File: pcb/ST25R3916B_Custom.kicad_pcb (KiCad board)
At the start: 2 copper layers, 40 x 40 mm, 12 parts

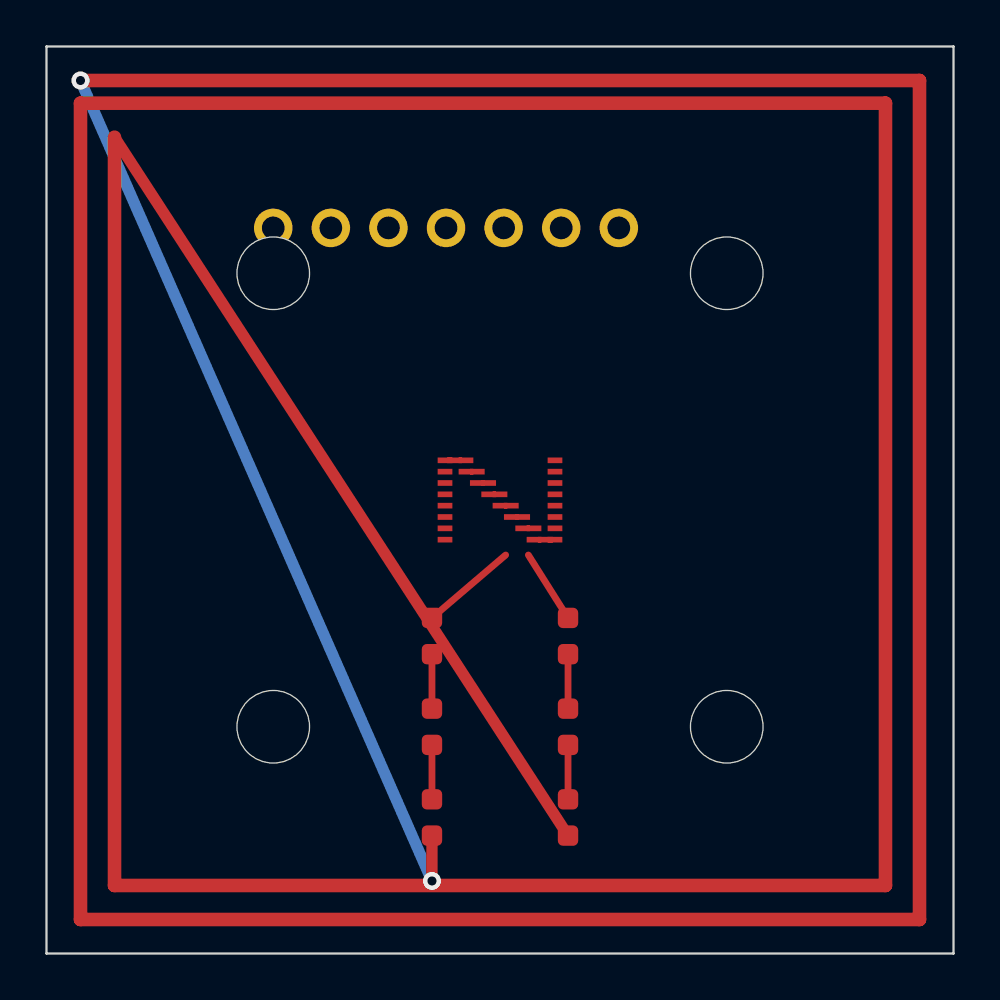
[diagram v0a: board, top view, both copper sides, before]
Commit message: feat(pcb): complete JLCPCB-ready PCB design with full PCBA outputs
- Fix generate_kicad.py: correct fp_text syntax for all footprints,
  add net declarations required by KiCad 7 parser
- Add all 22 SMD components with correct footprints and routing:
  RF matching network, crystal, LDO, bypass caps, SPI connector
- Replace broken legacy gerbers with clean kicad-cli exports
  (.gtl/.gbl/.gts/.gbs/.gto/.gbo/.gm1 + .drl)
- Add gerbers.zip ready for JLCPCB upload
- Add jlcpcb_bom.csv and jlcpcb_cpl.csv for PCBA ordering
- Update README with complete ordering instructions and pinout

Co-Authored-By: Claude Sonnet 4.6 <noreply@anthropic.com>
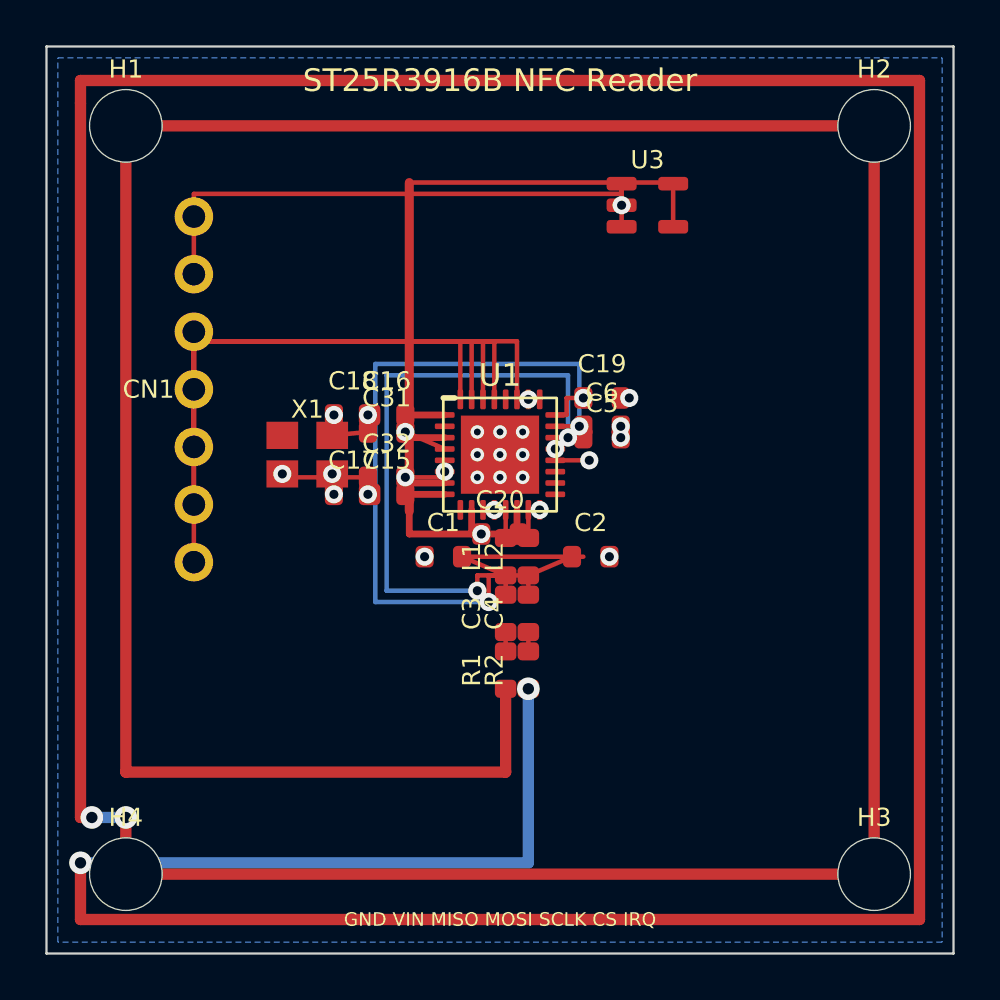
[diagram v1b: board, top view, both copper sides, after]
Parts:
- removed ? (x4): , MountingHole:MountingHole_3.2mm_M3
- removed ? (x6): , Resistor_SMD:R_0603_1608Metric
- removed ?: , Custom:ST25R3916B
- removed ?: , Connector_PinHeader_2.54mm:PinHeader_1x07_P2.54mm_Vertical
- added C1: 220pF, Resistor_SMD:R_0603_1608Metric, F.Cu at (117.5, 122.5)
- added C15: 100nF, Resistor_SMD:R_0603_1608Metric, F.Cu at (115.0, 119.8)
- added C16: 100nF, Resistor_SMD:R_0603_1608Metric, F.Cu at (115.0, 116.2)
- added C17: 2.2uF, Resistor_SMD:R_0603_1608Metric, F.Cu at (113.5, 119.8)
- added C18: 2.2uF, Resistor_SMD:R_0603_1608Metric, F.Cu at (113.5, 116.2)
- added C19: 10nF, Resistor_SMD:R_0603_1608Metric, F.Cu at (124.5, 115.5)
- added C2: 220pF, Resistor_SMD:R_0603_1608Metric, F.Cu at (124.0, 122.5)
- added C20: 10nF, Resistor_SMD:R_0603_1608Metric, F.Cu at (120.0, 121.5)
- added C3: 120pF, Resistor_SMD:R_0603_1608Metric, F.Cu at (120.2, 125.0)
- added C31: 12pF, Resistor_SMD:R_0603_1608Metric, F.Cu at (115.0, 117.0)
- added C32: 12pF, Resistor_SMD:R_0603_1608Metric, F.Cu at (115.0, 119.0)
- added C4: 120pF, Resistor_SMD:R_0603_1608Metric, F.Cu at (121.2, 125.0)
- added C5: 180pF, Resistor_SMD:R_0603_1608Metric, F.Cu at (124.5, 117.2)
- added C6: 180pF, Resistor_SMD:R_0603_1608Metric, F.Cu at (124.5, 116.8)
- added CN1: 7P-2.54mm, Connector_PinHeader_2.54mm:PinHeader_1x07_P2.54mm_Vertical, F.Cu at (106.5, 107.5)
- added H1: M3, MountingHole:MountingHole_3.2mm_M3, F.Cu at (103.5, 103.5)
- added H2: M3, MountingHole:MountingHole_3.2mm_M3, F.Cu at (136.5, 103.5)
- added H3: M3, MountingHole:MountingHole_3.2mm_M3, F.Cu at (136.5, 136.5)
- added H4: M3, MountingHole:MountingHole_3.2mm_M3, F.Cu at (103.5, 136.5)
- added L1: 270nH, Resistor_SMD:R_0603_1608Metric, F.Cu at (120.2, 122.5)
- added L2: 270nH, Resistor_SMD:R_0603_1608Metric, F.Cu at (121.2, 122.5)
- added R1: 2.2R, Resistor_SMD:R_0603_1608Metric, F.Cu at (120.2, 127.5)
- added R2: 2.2R, Resistor_SMD:R_0603_1608Metric, F.Cu at (121.2, 127.5)
- added U1: ST25R3916B, Package_DFN_QFN:QFN-32-1EP_5x5mm_P0.5mm_EP3.45x3.45mm, F.Cu at (120.0, 118.0)
- added U3: 3V3_LDO, Package_TO_SOT_SMD:SOT-23-5, F.Cu at (126.5, 107.0)
- added X1: 27.12MHz, Crystal:Crystal_SMD_3225-4Pin_3.2x2.5mm, F.Cu at (111.5, 118.0)
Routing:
- net (no net): track 378.4 -> 583.6 mm, vias 2 -> 40
- added copper zone on B.Cu, net GND
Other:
- board text added: "GND VIN MISO MOSI SCLK CS IRQ"
- board text added: "ST25R3916B NFC Reader"

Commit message: fix(pcb): fix all layout issues — centered IC, no overlaps, antenna on board
- IC moved to (120,120): dead-center of 40x40mm board
- Remove mounting holes: were exactly on inner antenna trace corners,
  causing antenna-through-drill conflicts
- Inner antenna offset increased 3.5->5mm: clears CN1 connector area,
  antenna now fully inside board with visible clearance on all sides
- Outer antenna offset 1.5->2mm: added margin from board edge
- All component overlaps fixed: proper 0.5mm+ pad-to-pad clearance
  throughout (L1/C20 overlap eliminated, C20/IC bottom DRC gap fixed)
- Crystal load caps C31/C32 repositioned to x=114.5 (clear of X1 body)
- Decoupling caps C15-C18 split above/below crystal zone to avoid conflicts
- RF matching L1/L2/C3/C4/R1/R2 spaced to 0.55mm+ clearance at each joint
- RFI shunt caps C5/C6/C19 at 1.5mm pitch (0.55mm pad gap)
- SPI traces use individual y-levels (112.0 to 110.4) to avoid VDD bus
- VDD bus routes at y=107.5 (above SPI zone) then down x=116.5 to IC pins
- Regenerate gerbers.zip and CPL with corrected coordinates

Co-Authored-By: Claude Sonnet 4.6 <noreply@anthropic.com>
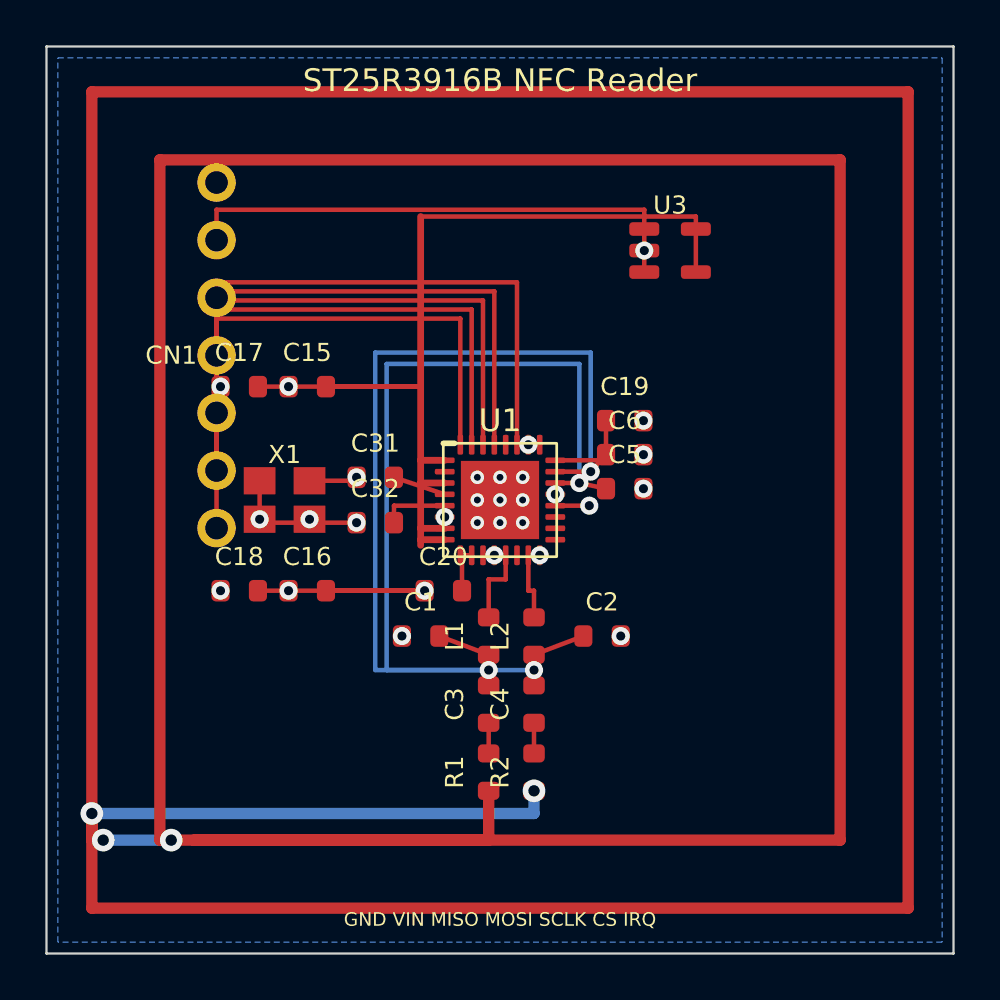
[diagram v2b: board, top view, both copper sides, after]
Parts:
- removed H1, H2, H3, H4: M3, MountingHole:MountingHole_3.2mm_M3
- moved C18 9.22 mm to (108.5, 124.0)
- moved C16 8.50 mm to (111.5, 124.0)
- moved C17 6.90 mm to (108.5, 115.0)
- moved C15 5.90 mm to (111.5, 115.0)
- moved R1 4.56 mm to (119.5, 132.0)
- moved R2 4.51 mm to (121.5, 132.0)
- moved C3 4.07 mm to (119.5, 129.0)
- moved C4 4.01 mm to (121.5, 129.0)
- moved C1 3.64 mm to (116.5, 126.0)
- moved L1 3.58 mm to (119.5, 126.0)
- moved C2 3.54 mm to (124.5, 126.0)
- moved C20 3.54 mm to (117.5, 124.0)
- moved L2 3.51 mm to (121.5, 126.0)
- moved C5 2.46 mm to (125.5, 119.5)
- moved U3 2.24 mm to (127.5, 109.0)
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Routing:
- net (no net): track 583.6 -> 612.4 mm, vias 40 -> 39

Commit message: fix(pcb): correct BOM component values from reference board analysis
- Inductors L1/L2: 270nH → 27nH (C148128, Murata LQW18AN27NG00D)
  Previous value was 10× too high (~23Ω series impedance at 13.56MHz);
  reference board (Elechouse cardboard) confirmed uses 27nH.
- Crystal load caps C31/C32: 12pF → 10pF (C1634) to match crystal spec
- Damping resistors R1/R2: fix wrong LCSC part C22935 (was 1MΩ!) → C22939 (2.2Ω)
- Regenerate PCB, Gerbers, BOM.md with corrected values

Co-Authored-By: Claude Sonnet 4.6 <noreply@anthropic.com>
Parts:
- C31, C32: value 12pF -> 10pF
- L1, L2: value 270nH -> 27nH
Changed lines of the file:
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@@
   (footprint "Resistor_SMD:R_0603_1608Metric" (layer "F.Cu") (at 114.5000 119.0000 0)
     (fp_text reference "C31" (at 0 -1.5 0) (layer "F.SilkS") (effects (font (size 0.8 0.8) (thickness 0.12))))
-    (fp_text value    "12pF"  (at 0  1.5 0) (layer "F.Fab")   (effects (font (size 0.8 0.8) (thickness 0.12))))
+    (fp_text value    "10pF"  (at 0  1.5 0) (layer "F.Fab")   (effects (font (size 0.8 0.8) (thickness 0.12))))
     (pad "1" smd roundrect (at -0.825 0 0) (size 0.8 0.95) (layers "F.Cu" "F.Paste" "F.Mask") (roundrect_rratio 0.25) (tstamp "TS0042"))
     (pad "2" smd roundrect (at  0.825 0 0) (size 0.8 0.95) (layers "F.Cu" "F.Paste" "F.Mask") (roundrect_rratio 0.25) (tstamp "TS0043"))
@@
   (footprint "Resistor_SMD:R_0603_1608Metric" (layer "F.Cu") (at 114.5000 121.0000 0)
     (fp_text reference "C32" (at 0 -1.5 0) (layer "F.SilkS") (effects (font (size 0.8 0.8) (thickness 0.12))))
-    (fp_text value    "12pF"  (at 0  1.5 0) (layer "F.Fab")   (effects (font (size 0.8 0.8) (thickness 0.12))))
+    (fp_text value    "10pF"  (at 0  1.5 0) (layer "F.Fab")   (effects (font (size 0.8 0.8) (thickness 0.12))))
     (pad "1" smd roundrect (at -0.825 0 0) (size 0.8 0.95) (layers "F.Cu" "F.Paste" "F.Mask") (roundrect_rratio 0.25) (tstamp "TS0044"))
     (pad "2" smd roundrect (at  0.825 0 0) (size 0.8 0.95) (layers "F.Cu" "F.Paste" "F.Mask") (roundrect_rratio 0.25) (tstamp "TS0045"))
@@
   (footprint "Resistor_SMD:R_0603_1608Metric" (layer "F.Cu") (at 119.5000 126.0000 90)
     (fp_text reference "L1" (at 0 -1.5 90) (layer "F.SilkS") (effects (font (size 0.8 0.8) (thickness 0.12))))
-    (fp_text value    "270nH"  (at 0  1.5 90) (layer "F.Fab")   (effects (font (size 0.8 0.8) (thickness 0.12))))
+    (fp_text value    "27nH"  (at 0  1.5 90) (layer "F.Fab")   (effects (font (size 0.8 0.8) (thickness 0.12))))
     (pad "1" smd roundrect (at -0.825 0 90) (size 0.8 0.95) (layers "F.Cu" "F.Paste" "F.Mask") (roundrect_rratio 0.25) (tstamp "TS0054"))
     (pad "2" smd roundrect (at  0.825 0 90) (size 0.8 0.95) (layers "F.Cu" "F.Paste" "F.Mask") (roundrect_rratio 0.25) (tstamp "TS0055"))
@@
   (footprint "Resistor_SMD:R_0603_1608Metric" (layer "F.Cu") (at 121.5000 126.0000 90)
     (fp_text reference "L2" (at 0 -1.5 90) (layer "F.SilkS") (effects (font (size 0.8 0.8) (thickness 0.12))))
-    (fp_text value    "270nH"  (at 0  1.5 90) (layer "F.Fab")   (effects (font (size 0.8 0.8) (thickness 0.12))))
+    (fp_text value    "27nH"  (at 0  1.5 90) (layer "F.Fab")   (effects (font (size 0.8 0.8) (thickness 0.12))))
     (pad "1" smd roundrect (at -0.825 0 90) (size 0.8 0.95) (layers "F.Cu" "F.Paste" "F.Mask") (roundrect_rratio 0.25) (tstamp "TS0056"))
     (pad "2" smd roundrect (at  0.825 0 90) (size 0.8 0.95) (layers "F.Cu" "F.Paste" "F.Mask") (roundrect_rratio 0.25) (tstamp "TS0057"))
